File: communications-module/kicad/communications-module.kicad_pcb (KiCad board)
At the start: 2 copper layers, 0 parts

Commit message: All schematics update
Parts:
- added REF**: MountingHole_3.2mm_M3, Mounting_Holes:MountingHole_3.2mm_M3, F.Cu at (146.3, 37.5)
- added REF**: MountingHole_3.2mm_M3, Mounting_Holes:MountingHole_3.2mm_M3, F.Cu at (66.0, 127.8)
- added REF**: MountingHole_3.2mm_M3, Mounting_Holes:MountingHole_3.2mm_M3, F.Cu at (226.6, 107.8)
- added REF**: MountingHole_3.2mm_M3, Mounting_Holes:MountingHole_3.2mm_M3, F.Cu at (226.6, 87.8)
- added REF**: MountingHole_3.2mm_M3, Mounting_Holes:MountingHole_3.2mm_M3, F.Cu at (226.6, 67.8)
- added REF**: MountingHole_3.2mm_M3, Mounting_Holes:MountingHole_3.2mm_M3, F.Cu at (226.6, 127.8)
- added REF**: MountingHole_3.2mm_M3, Mounting_Holes:MountingHole_3.2mm_M3, F.Cu at (146.3, 158.1)
- added REF**: MountingHole_3.2mm_M3, Mounting_Holes:MountingHole_3.2mm_M3, F.Cu at (66.0, 87.8)
- added REF**: MountingHole_3.2mm_M3, Mounting_Holes:MountingHole_3.2mm_M3, F.Cu at (66.0, 107.8)
- added REF**: MountingHole_3.2mm_M3, Mounting_Holes:MountingHole_3.2mm_M3, F.Cu at (183.8, 37.5)
- added REF**: MountingHole_3.2mm_M3, Mounting_Holes:MountingHole_3.2mm_M3, F.Cu at (183.8, 158.1)
- added REF**: MountingHole_3.2mm_M3, Mounting_Holes:MountingHole_3.2mm_M3, F.Cu at (108.8, 158.1)
- added REF**: MountingHole_3.2mm_M3, Mounting_Holes:MountingHole_3.2mm_M3, F.Cu at (108.8, 37.5)
- added REF**: MountingHole_3.2mm_M3, Mounting_Holes:MountingHole_3.2mm_M3, F.Cu at (66.0, 67.8)
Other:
- board outline added: 131.6 x 135.3 mm

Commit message: All gerbers update
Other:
- board size 131.6 x 135.3 mm -> 125.8 x 128.6 mm

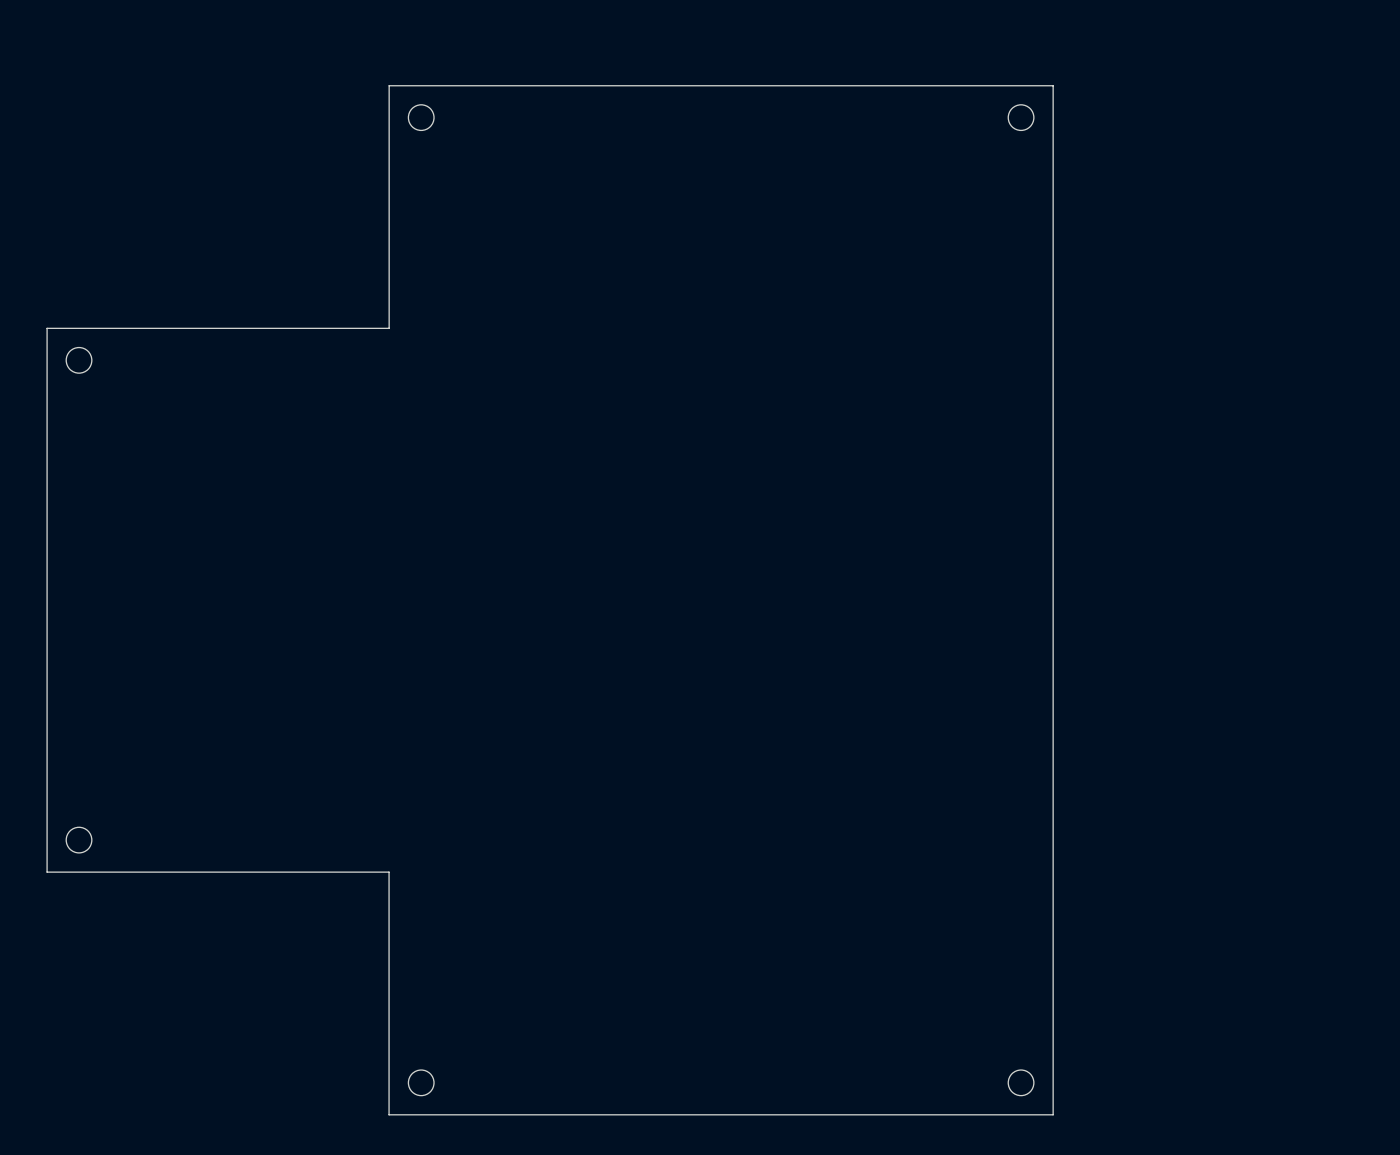
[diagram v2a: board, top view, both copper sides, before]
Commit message: Communications Module PCB components placed
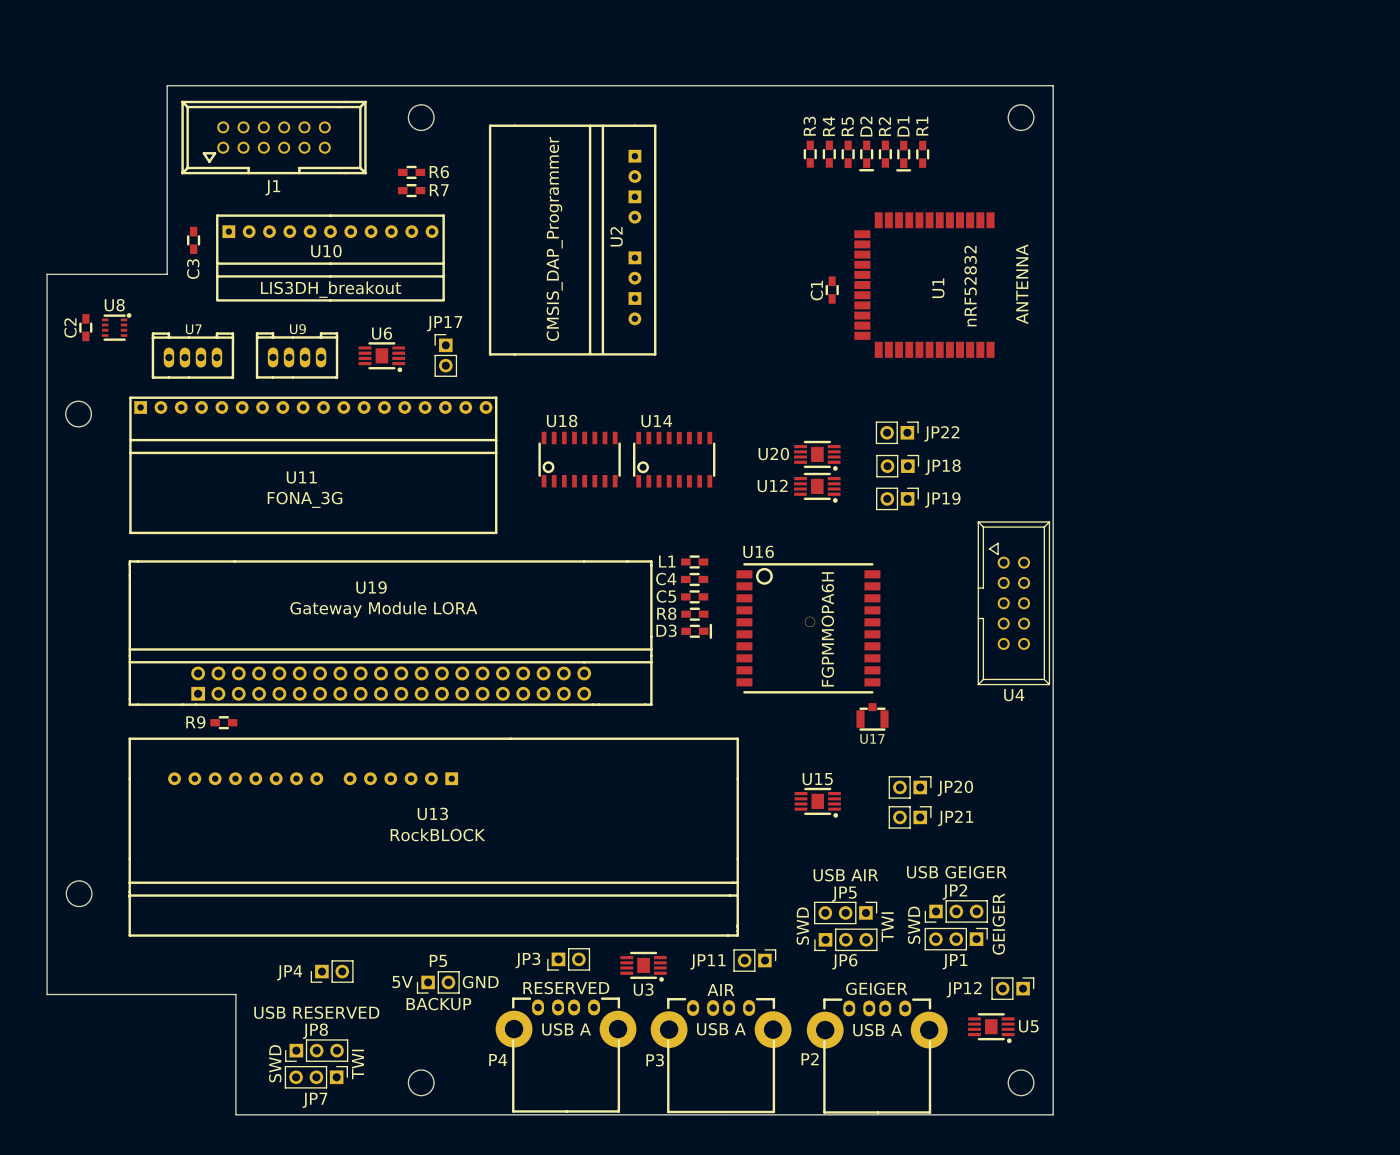
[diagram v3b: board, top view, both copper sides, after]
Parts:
- added C1: 100nF, 0603_handsolder:0603_HandSoldering, F.Cu at (160.2, 59.0)
- added C2: 100nF, 0603_handsolder:0603_HandSoldering, F.Cu at (66.9, 63.7)
- added C3: 100nF, 0603_handsolder:0603_HandSoldering, F.Cu at (80.3, 52.8)
- added C4: 1uF, 0603_handsolder:0603_HandSoldering, F.Cu at (143.0, 95.2)
- added C5: 100nF, 0603_handsolder:0603_HandSoldering, F.Cu at (143.0, 97.4)
- added D1: LED, 0603_handsolder:LED_0603_HandSoldering, F.Cu at (169.1, 42.1)
- added D2: LED, 0603_handsolder:LED_0603_HandSoldering, F.Cu at (164.5, 42.0)
- added D3: LED, 0603_handsolder:LED_0603_HandSoldering, F.Cu at (143.0, 101.7)
- added J1: IDC12, IDC12_connector:IDC12_connector, F.Cu at (89.1, 40.0)
- added JP1: JUMPER3, Socket_Strips:Socket_Strip_Straight_1x03_Pitch2.54mm, F.Cu at (178.2, 140.2)
- added JP11: Jumper_NC_Small, Socket_Strips:Socket_Strip_Straight_1x02_Pitch2.54mm, F.Cu at (151.8, 142.8)
- added JP12: Jumper_NC_Small, Socket_Strips:Socket_Strip_Straight_1x02_Pitch2.54mm, F.Cu at (184.0, 146.3)
- added JP17: Jumper_NC_Small, Socket_Strips:Socket_Strip_Straight_1x02_Pitch2.54mm, F.Cu at (111.9, 65.9)
- added JP18: Jumper_NC_Small, Socket_Strips:Socket_Strip_Straight_1x02_Pitch2.54mm, F.Cu at (169.6, 81.0)
- added JP19: Jumper_NC_Small, Socket_Strips:Socket_Strip_Straight_1x02_Pitch2.54mm, F.Cu at (169.6, 85.1)
- added JP2: JUMPER3, Socket_Strips:Socket_Strip_Straight_1x03_Pitch2.54mm, F.Cu at (173.1, 136.7)
- added JP20: Jumper_NC_Small, Socket_Strips:Socket_Strip_Straight_1x02_Pitch2.54mm, F.Cu at (171.2, 121.2)
- added JP21: Jumper_NC_Small, Socket_Strips:Socket_Strip_Straight_1x02_Pitch2.54mm, F.Cu at (171.2, 124.9)
- added JP22: Jumper_NC_Small, Socket_Strips:Socket_Strip_Straight_1x02_Pitch2.54mm, F.Cu at (169.6, 76.9)
- added JP3: Jumper_NC_Small, Socket_Strips:Socket_Strip_Straight_1x02_Pitch2.54mm, F.Cu at (126.0, 142.7)
- added JP4: Jumper_NC_Small, Socket_Strips:Socket_Strip_Straight_1x02_Pitch2.54mm, F.Cu at (96.4, 144.2)
- added JP5: JUMPER3, Socket_Strips:Socket_Strip_Straight_1x03_Pitch2.54mm, F.Cu at (164.4, 136.9)
- added JP6: JUMPER3, Socket_Strips:Socket_Strip_Straight_1x03_Pitch2.54mm, F.Cu at (159.3, 140.2)
- added JP7: JUMPER3, Socket_Strips:Socket_Strip_Straight_1x03_Pitch2.54mm, F.Cu at (98.2, 157.4)
- added JP8: JUMPER3, Socket_Strips:Socket_Strip_Straight_1x03_Pitch2.54mm, F.Cu at (93.2, 154.1)
- added L1: FERRITE, 0603_handsolder:0603_HandSoldering, F.Cu at (143.0, 93.0)
- added P2: USB_A, USB_A_receptacle:USB_A_receptacle, F.Cu at (165.8, 148.8)
- added P3: USB_A, USB_A_receptacle:USB_A_receptacle, F.Cu at (146.3, 148.8)
- added P4: USB_A, USB_A_receptacle:USB_A_receptacle, F.Cu at (126.9, 148.7)
- added P5: BACKUP, Socket_Strips:Socket_Strip_Straight_1x02_Pitch2.54mm, F.Cu at (109.7, 145.6)
- added R1: 1K, 0603_handsolder:0603_HandSoldering, F.Cu at (171.5, 42.1)
- added R2: 1K, 0603_handsolder:0603_HandSoldering, F.Cu at (166.8, 42.0)
- added R3: 10K, 0603_handsolder:0603_HandSoldering, F.Cu at (157.4, 42.0)
- added R4: 10K, 0603_handsolder:0603_HandSoldering, F.Cu at (159.8, 42.0)
- added R5: 10K, 0603_handsolder:0603_HandSoldering, F.Cu at (162.2, 42.0)
- added R6: 0R, 0603_handsolder:0603_HandSoldering, F.Cu at (107.6, 44.3)
- added R7: 0R, 0603_handsolder:0603_HandSoldering, F.Cu at (107.6, 46.6)
- added R8: 1K, 0603_handsolder:0603_HandSoldering, F.Cu at (143.0, 99.5)
- added R9: 10K, 0603_handsolder:0603_HandSoldering, F.Cu at (84.1, 113.1)
- added U1: nRF52832, nRF52832:nRF52832-SMD, F.Cu at (166.0, 50.3)
- added U10: LIS3DH_breakout, LIS3DH_breakout:LIS3DH_breakout_vertical, F.Cu at (97.5, 46.7)
- added U11: FONA_3G, FONA_3G:FONA_3G_vertical, F.Cu at (72.5, 75.5)
- added U12: TPS2064, TPS2064:TPS2064, F.Cu at (158.3, 83.6)
- added U13: RockBLOCK, RockBlock:RockBlock_vertical, F.Cu at (72.4, 120.1)
- added U14: SN74LV4052A, SN74LV4052A:SN74LV4052A, F.Cu at (140.4, 80.2)
- added U15: TPS2064, TPS2064:TPS2064, F.Cu at (158.4, 122.9)
- added U16: FGPMMOPA6H, FGPMMOPA6H_GPS:FGPMMOPA6H_GPS, F.Cu at (149.2, 109.3)
- added U17: uFL_conn, UFL-R-SMT:U.FL-R-SMT, F.Cu at (165.2, 112.7)
- added U18: SN74LV4052A, SN74LV4052A:SN74LV4052A, F.Cu at (128.6, 80.2)
- added U19: Gateway Module LORA, Solarcast_Gateway_Module:Solarcast_Gateway_Module, F.Cu at (129.2, 106.9)
- added U2: CMSIS_DAP_Programmer, CMSIS_DAP_Breakout:CMSIS_DAP_Breakout, F.Cu at (135.5, 42.3)
- added U20: TPS2064, TPS2064:TPS2064, F.Cu at (158.3, 79.6)
- added U3: TPS2064, TPS2064:TPS2064, F.Cu at (136.6, 143.4)
- added U4: PWR_CONN, IDC10_connector:IDC10_connector, F.Cu at (182.9, 98.2)
- added U5: TPS2064, TPS2064:TPS2064, F.Cu at (180.1, 151.1)
- added U6: TPS2064, TPS2064:TPS2064, F.Cu at (103.9, 67.2)
- added U7: I2C_connector, DIP Grove 4P-2.0:DIP_Grove_4P-2_0, F.Cu at (77.3, 67.5)
- added U8: BME280, BME280:BME280, F.Cu at (69.2, 65.0)
- added U9: I2C_connector, DIP Grove 4P-2.0:DIP_Grove_4P-2_0, F.Cu at (90.3, 67.4)
- moved REF** 6.71 mm to (66.0, 74.5)
- moved REF** 6.71 mm to (226.6, 94.5)
- moved REF** 6.71 mm to (226.6, 74.5)
- moved REF** 6.71 mm to (226.6, 114.5)
- moved REF** 6.71 mm to (66.0, 94.5)
- moved REF** 6.70 mm to (66.0, 114.5)
- moved REF** 6.70 mm to (66.0, 134.5)
- moved REF** 6.70 mm to (226.6, 134.5)
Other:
- outline, holes or cut-outs redrawn
- board text added: "5V"
- board text added: "AIR"
- board text added: "GEIGER"
- board text added: "GND"
- board text added: "RESERVED"
- board text added: "SWD"
- board text added: "TWI"
- board text added: "USB AIR"
- board text added: "USB GEIGER"
- board text added: "USB RESERVED"

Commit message: Communications Module PCB update
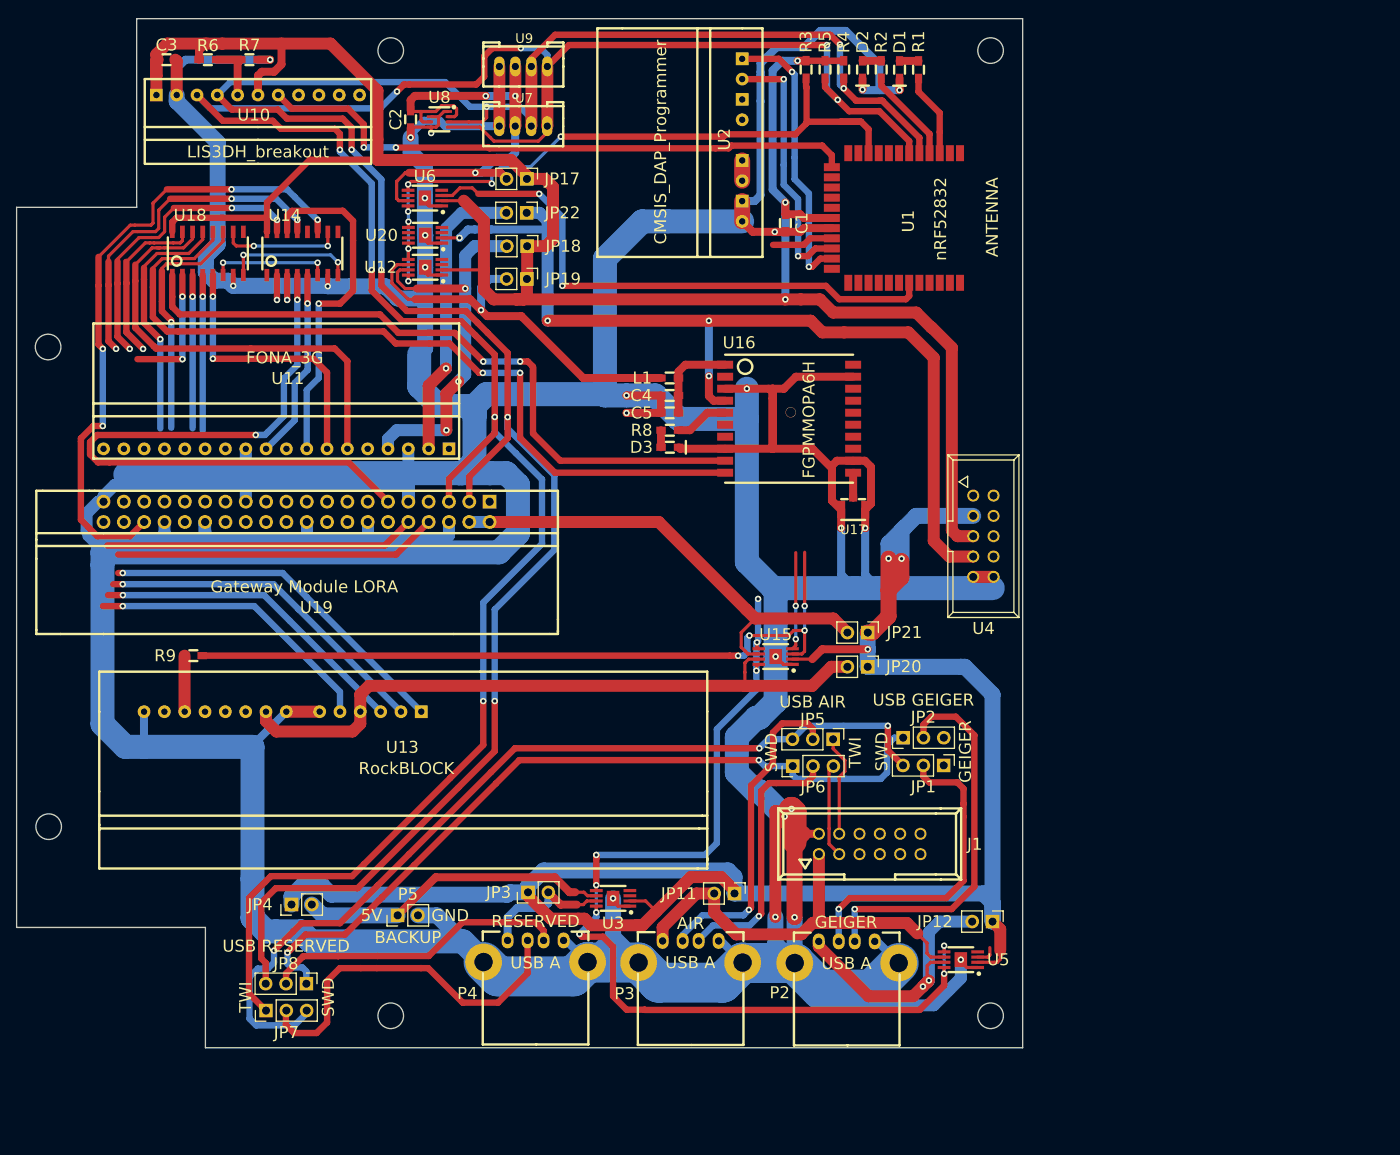
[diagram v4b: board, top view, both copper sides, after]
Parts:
- moved J1 115.5 mm to (163.6, 128.3)
- moved U19 63.0 mm to (69.1, 88.0), turned to 270 degrees
- moved U12 56.2 mm to (109.3, 56.2)
- moved U20 56.2 mm to (109.3, 52.2)
- moved JP19 55.0 mm to (122.0, 57.6)
- moved JP22 55.0 mm to (122.0, 49.4)
- moved JP18 55.0 mm to (122.0, 53.5)
- moved U14 53.1 mm to (93.9, 54.4)
- moved U18 53.1 mm to (82.1, 54.4)
- moved U7 50.4 mm to (118.6, 38.5)
- moved C2 48.2 mm to (107.5, 37.7)
- moved U8 48.2 mm to (109.8, 38.9)
- moved U9 46.1 mm to (118.6, 31.1)
- moved U11 41.1 mm to (113.5, 77.1), turned to 180 degrees
- moved R6 29.1 mm to (82.1, 30.2), turned to 0 degrees
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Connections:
- U1 pad 11: Net-(U1-Pad11) -> ENABLE-RESERV
- U1 pad 12: Net-(U1-Pad12) -> (no net)
- U1 pad 24: ENABLE-3V3 -> ENABLE-BACKUP
- U10 pad 10: Net-(U10-Pad10) -> (no net)
- U10 pad 11: Net-(U10-Pad11) -> (no net)
- U10 pad 8: Net-(U10-Pad8) -> (no net)
- U10 pad 9: Net-(U10-Pad9) -> (no net)
- U11 pad 1: Net-(U11-Pad1) -> (no net)
- U11 pad 12: Net-(U11-Pad12) -> (no net)
- U11 pad 13: Net-(U11-Pad13) -> (no net)
- U11 pad 14: Net-(U11-Pad14) -> (no net)
- U11 pad 15: Net-(U11-Pad15) -> (no net)
- U11 pad 16: Net-(U11-Pad16) -> (no net)
- U11 pad 17: Net-(U11-Pad17) -> (no net)
- U11 pad 18: Net-(U11-Pad18) -> (no net)
- U11 pad 5: Net-(U11-Pad5) -> (no net)
- U11 pad 9: Net-(U11-Pad9) -> (no net)
- U13 pad 10: Net-(U13-Pad10) -> (no net)
- U13 pad 11: Net-(U13-Pad11) -> (no net)
- U13 pad 13: Net-(U13-Pad13) -> (no net)
- U13 pad 9: Net-(U13-Pad9) -> (no net)
- U14 pad 1: Net-(U14-Pad1) -> (no net)
- U14 pad 12: Net-(U14-Pad12) -> (no net)
- U16 pad 13: Net-(U16-Pad13) -> (no net)
- U16 pad 14: Net-(U16-Pad14) -> (no net)
- U16 pad 15: Net-(U16-Pad15) -> (no net)
- U16 pad 16: Net-(U16-Pad16) -> (no net)
- U16 pad 17: Net-(U16-Pad17) -> (no net)
- U16 pad 18: Net-(U16-Pad18) -> (no net)
- U16 pad 2: Net-(U16-Pad2) -> (no net)
- U16 pad 20: Net-(U16-Pad20) -> (no net)
- U16 pad 6: Net-(U16-Pad6) -> (no net)
- U16 pad 7: Net-(U16-Pad7) -> (no net)
- U19 pad 1: Net-(U19-Pad1) -> (no net)
- U19 pad 12: Net-(U19-Pad12) -> (no net)
- U19 pad 13: Net-(U19-Pad13) -> (no net)
- U19 pad 15: Net-(U19-Pad15) -> (no net)
- U19 pad 16: Net-(U19-Pad16) -> (no net)
- U19 pad 17: Net-(U19-Pad17) -> (no net)
- U19 pad 18: Net-(U19-Pad18) -> (no net)
- U19 pad 19: Net-(U19-Pad19) -> (no net)
- U19 pad 21: Net-(U19-Pad21) -> (no net)
- U19 pad 22: Net-(U19-Pad22) -> (no net)
- U19 pad 23: Net-(U19-Pad23) -> (no net)
- U19 pad 24: Net-(U19-Pad24) -> (no net)
- U19 pad 26: Net-(U19-Pad26) -> (no net)
- U19 pad 27: Net-(U19-Pad27) -> (no net)
- U19 pad 28: Net-(U19-Pad28) -> (no net)
- U19 pad 29: Net-(U19-Pad29) -> (no net)
- U19 pad 31: Net-(U19-Pad31) -> (no net)
- U19 pad 32: Net-(U19-Pad32) -> (no net)
- U19 pad 33: Net-(U19-Pad33) -> (no net)
- U19 pad 35: Net-(U19-Pad35) -> (no net)
- U19 pad 37: Net-(U19-Pad37) -> (no net)
- U19 pad 38: Net-(U19-Pad38) -> (no net)
- U19 pad 40: Net-(U19-Pad40) -> (no net)
- U19 pad 7: Net-(U19-Pad7) -> (no net)
- U2 pad 3: Net-(U2-Pad3) -> (no net)
- U2 pad 4: Net-(U2-Pad4) -> (no net)
- U20 pad 4: Net-(U20-Pad4) -> (no net)
- U20 pad 6: Net-(U20-Pad6) -> (no net)
- U4 pad 6: ENABLE-3V3 -> (no net)
- U5 pad 3: ENABLE-AIR -> ENABLE-GEIG
- U5 pad 4: ENABLE-GEIG -> ENABLE-AIR
- U5 pad 6: GEIGER_5V -> AIR_5V
- U5 pad 7: AIR_5V -> GEIGER_5V
- U6 pad 4: Net-(U6-Pad4) -> (no net)
- U6 pad 6: Net-(U6-Pad6) -> (no net)
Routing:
- net GND: track 0.00 -> 1001.3 mm, vias 0 -> 24
- net TWI_SCL: track 0.00 -> 324.1 mm, vias 0 -> 8
- net TWI_SDA: track 0.00 -> 305.3 mm, vias 0 -> 7
- net +3V3: track 0.00 -> 285.5 mm, vias 0 -> 3
- net +5V: track 0.00 -> 232.9 mm, vias 0 -> 3
- net PWR_SWITCH_OC: track 0.00 -> 213.7 mm, vias 0 -> 16
- net NRF_SWCLK: track 0.00 -> 146.2 mm, vias 0 -> 5
- net NRF_SWDIO: track 0.00 -> 135.6 mm, vias 0 -> 4
- net VBAT: track 0.00 -> 120.3 mm, vias 0 -> 4
- net GPS_TX: track 0.00 -> 100.5 mm, vias 0 -> 2
- net ENABLE-ROCK: track 0.00 -> 91.7 mm, vias 0 -> 4
- net GPS_RX: track 0.00 -> 88.2 mm, vias 0 -> 2
- net LORA_RTS: track 0.00 -> 85.1 mm, vias 0 -> 2
- net ROCK_5V: track 0.00 -> 84.7 mm
- net LORA_CTS: track 0.00 -> 79.8 mm, vias 0 -> 4
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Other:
- net class Default: clearance 0.2 -> 0.1778; trace_width 0.25 -> 0.1778; via_dia 0.6 -> 0.8
- rule trace_clearance: 0.2 -> 0.1778
- rule trace_min: 0.2 -> 0.1778
- rule via_min_drill: 0.3 -> 0.4
- rule via_min_size: 0.4 -> 0.8
